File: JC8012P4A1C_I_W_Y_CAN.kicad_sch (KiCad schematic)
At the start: 16 parts, among them J1 610110249121, J2 68711414522, J3 653104131822, U1 TLE9250VSJ

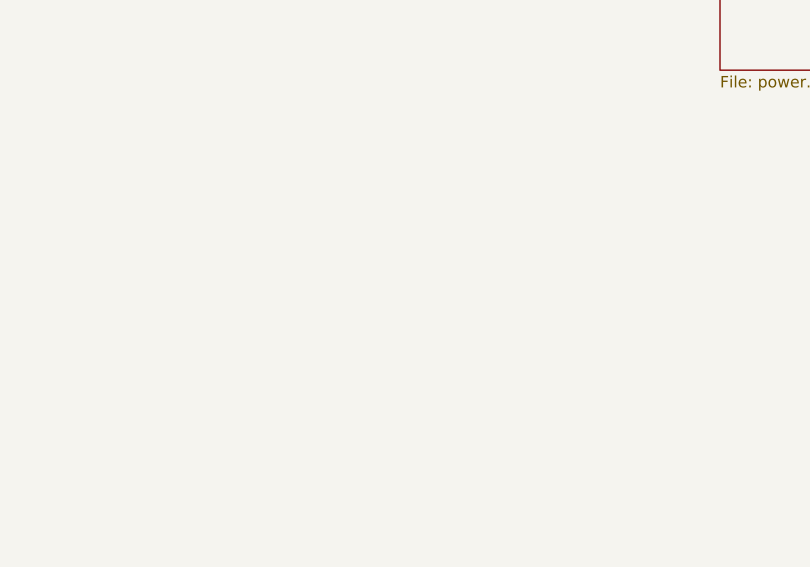
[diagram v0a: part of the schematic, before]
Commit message: Test points TP1-TP5 in the schematic
TP1 +5V, TP2 GND, TP3 CAN_H, TP4 CAN_L (main sheet), TP5 VIN_PROT
(12 V after fuse and reverse polarity protection, power sheet).
Footprint TestPoint_Pad_D1.5mm (SMD). Not yet on the PCB (F8).

Co-Authored-By: Claude Opus 5.5 <noreply@anthropic.com>
Claude-Session: https://claude.ai/code/session_014h8cGi8SRWthYdGFH1Qgzz
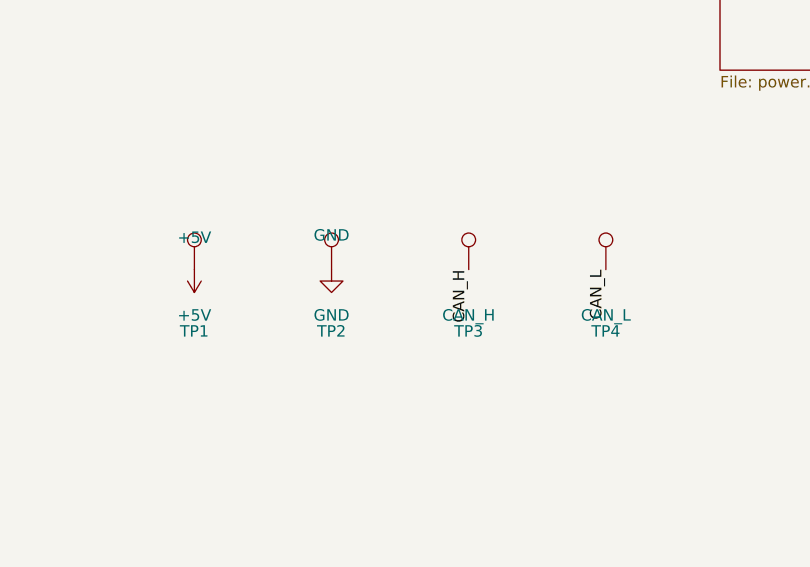
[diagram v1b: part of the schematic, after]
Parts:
- added TP1: +5V, TestPoint:TestPoint_Pad_D1.5mm, symbol Connector:TestPoint
- added TP2: GND, TestPoint:TestPoint_Pad_D1.5mm, symbol Connector:TestPoint
- added TP3: CAN_H, TestPoint:TestPoint_Pad_D1.5mm, symbol Connector:TestPoint
- added TP4: CAN_L, TestPoint:TestPoint_Pad_D1.5mm, symbol Connector:TestPoint
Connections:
- net +5V: now also TP1.1
- net CAN_H: now also TP3.1
- net CAN_L: now also TP4.1
- net GND: now also TP2.1

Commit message: Test points excluded from BOM, README: hand assembly, stencil, BOM export
Co-Authored-By: Claude Opus 5.5 <noreply@anthropic.com>
Claude-Session: https://claude.ai/code/session_014h8cGi8SRWthYdGFH1Qgzz
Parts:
- TP1, TP2, TP3, TP4: now left out of the parts list
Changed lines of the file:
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@@
 		(body_style 1)
 		(exclude_from_sim no)
-		(in_bom yes)
+		(in_bom no)
 		(on_board yes)
 		(in_pos_files yes)
@@
 		(body_style 1)
 		(exclude_from_sim no)
-		(in_bom yes)
+		(in_bom no)
 		(on_board yes)
 		(in_pos_files yes)
@@
 		(body_style 1)
 		(exclude_from_sim no)
-		(in_bom yes)
+		(in_bom no)
 		(on_board yes)
 		(in_pos_files yes)
@@
 		(body_style 1)
 		(exclude_from_sim no)
-		(in_bom yes)
-		(on_board yes)
-		(in_pos_files yes)
+		(in_bom no)
+		(on_board yes)
+		(in_pos_files yes)

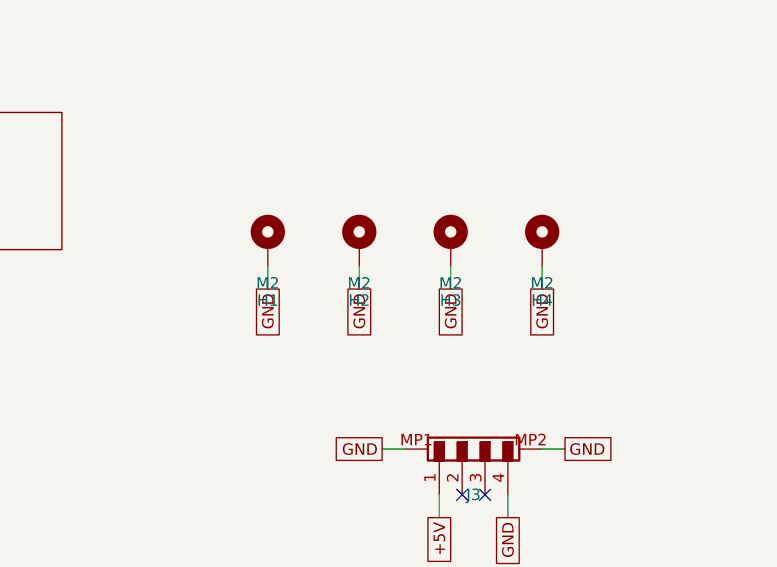
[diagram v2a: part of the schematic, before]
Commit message: Mounting holes H1-H4 replaced by SMD steel spacers Wurth 9774025943R (2.5 mm, M2x6)
Co-Authored-By: Claude Opus 5.5 <noreply@anthropic.com>
Claude-Session: https://claude.ai/code/session_014h8cGi8SRWthYdGFH1Qgzz
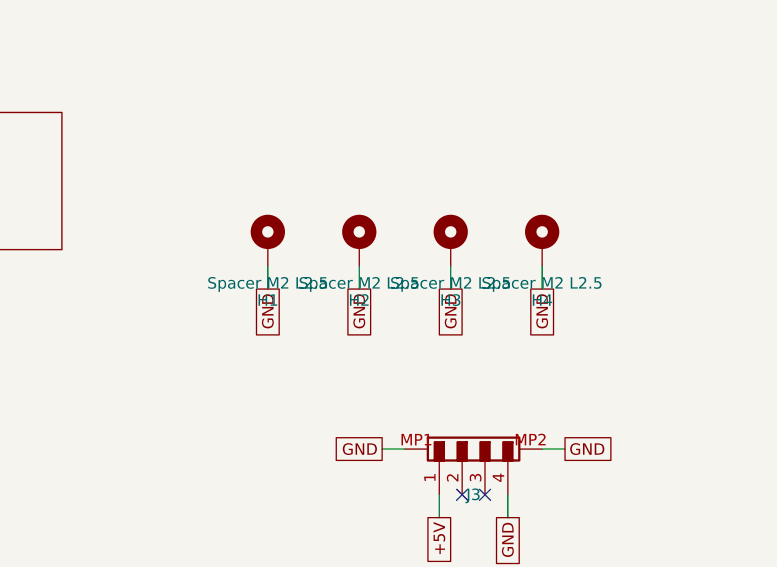
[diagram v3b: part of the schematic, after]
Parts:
- H1, H2, H3, H4: value M2 -> Spacer M2 L2.5; footprint MountingHole:MountingHole_2.2mm_M2_Pad_Via -> JC8012P4A1C_CAN:A_Wurth_WA-SMST_9774025943R; MPN (none) -> 9774025943R; Manufacturer (none) -> Wurth Elektronik; now in the parts list
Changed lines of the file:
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@@
 		(body_style 1)
 		(exclude_from_sim no)
-		(in_bom no)
+		(in_bom yes)
 		(on_board yes)
 		(in_pos_files no)
@@
 			)
 		)
-		(property "Value" "M2"
+		(property "Value" "Spacer M2 L2.5"
 			(at 213.36 133.985 0)
 			(show_name no)
@@
 			)
 		)
-		(property "Footprint" "MountingHole:MountingHole_2.2mm_M2_Pad_Via"
+		(property "Footprint" "JC8012P4A1C_CAN:A_Wurth_WA-SMST_9774025943R"
 			(at 213.36 129.54 0)
 			(hide yes)
@@
 			)
 		)
-		(property "Description" "Mounting Hole with connection"
-			(at 213.36 129.54 0)
-			(hide yes)
-			(show_name no)
-			(do_not_autoplace no)
-			(effects
-				(font
-					(size 1.27 1.27)
-				)
+		(property "Description" "SMD steel spacer, through hole 2.25 mm, L 2.5 mm, for M2x6 screw"
+			(at 213.36 129.54 0)
+			(hide yes)
+			(show_name no)
+			(do_not_autoplace no)
+			(effects
+				(font
+					(size 1.27 1.27)
+				)
+			)
+		)
+		(property "MPN" "9774025943R"
+			(at 213.36 129.54 0)
+			(effects
+				(font
+					(size 1.27 1.27)
+				)
+				(hide yes)
+			)
+		)
+		(property "Manufacturer" "Wurth Elektronik"
+			(at 213.36 129.54 0)
+			(effects
+				(font
+					(size 1.27 1.27)
+				)
+				(hide yes)
 			)
 		)
@@
 		(body_style 1)
 		(exclude_from_sim no)
-		(in_bom no)
+		(in_bom yes)
 		(on_board yes)
 		(in_pos_files no)
@@
 			)
 		)
-		(property "Value" "M2"
+		(property "Value" "Spacer M2 L2.5"
 			(at 223.52 133.985 0)
 			(show_name no)
@@
 			)
 		)
-		(property "Footprint" "MountingHole:MountingHole_2.2mm_M2_Pad_Via"
+		(property "Footprint" "JC8012P4A1C_CAN:A_Wurth_WA-SMST_9774025943R"
 			(at 223.52 129.54 0)
 			(hide yes)
@@
 			)
 		)
-		(property "Description" "Mounting Hole with connection"
-			(at 223.52 129.54 0)
-			(hide yes)
-			(show_name no)
-			(do_not_autoplace no)
-			(effects
-				(font
-					(size 1.27 1.27)
-				)
+		(property "Description" "SMD steel spacer, through hole 2.25 mm, L 2.5 mm, for M2x6 screw"
+			(at 223.52 129.54 0)
+			(hide yes)
+			(show_name no)
+			(do_not_autoplace no)
+			(effects
+				(font
+					(size 1.27 1.27)
+				)
+			)
+		)
+		(property "MPN" "9774025943R"
+			(at 223.52 129.54 0)
+			(effects
+				(font
+					(size 1.27 1.27)
+				)
+				(hide yes)
+			)
+		)
+		(property "Manufacturer" "Wurth Elektronik"
+			(at 223.52 129.54 0)
+			(effects
+				(font
+					(size 1.27 1.27)
+				)
+				(hide yes)
 			)
 		)
@@
 		(body_style 1)
 		(exclude_from_sim no)
-		(in_bom no)
+		(in_bom yes)
 		(on_board yes)
 		(in_pos_files no)
@@
 			)
 		)
-		(property "Value" "M2"
+		(property "Value" "Spacer M2 L2.5"
 			(at 233.68 133.985 0)
 			(show_name no)
@@
 			)
 		)
-		(property "Footprint" "MountingHole:MountingHole_2.2mm_M2_Pad_Via"
+		(property "Footprint" "JC8012P4A1C_CAN:A_Wurth_WA-SMST_9774025943R"
 			(at 233.68 129.54 0)
 			(hide yes)
@@
 			)
 		)
-		(property "Description" "Mounting Hole with connection"
-			(at 233.68 129.54 0)
-			(hide yes)
-			(show_name no)
-			(do_not_autoplace no)
-			(effects
-				(font
-					(size 1.27 1.27)
-				)
+		(property "Description" "SMD steel spacer, through hole 2.25 mm, L 2.5 mm, for M2x6 screw"
+			(at 233.68 129.54 0)
+			(hide yes)
+			(show_name no)
+			(do_not_autoplace no)
+			(effects
+				(font
+					(size 1.27 1.27)
+				)
+			)
+		)
+		(property "MPN" "9774025943R"
+			(at 233.68 129.54 0)
+			(effects
+				(font
+					(size 1.27 1.27)
+				)
+				(hide yes)
+			)
+		)
+		(property "Manufacturer" "Wurth Elektronik"
+			(at 233.68 129.54 0)
+			(effects
+				(font
+					(size 1.27 1.27)
+				)
+				(hide yes)
 			)
 		)
@@
 		(body_style 1)
 		(exclude_from_sim no)
-		(in_bom no)
+		(in_bom yes)
 		(on_board yes)
 		(in_pos_files no)
@@
 			)
 		)
-		(property "Value" "M2"
+		(property "Value" "Spacer M2 L2.5"
 			(at 243.84 133.985 0)
 			(show_name no)
@@
 			)
 		)
-		(property "Footprint" "MountingHole:MountingHole_2.2mm_M2_Pad_Via"
+		(property "Footprint" "JC8012P4A1C_CAN:A_Wurth_WA-SMST_9774025943R"
 			(at 243.84 129.54 0)
 			(hide yes)
@@
 			)
 		)
-		(property "Description" "Mounting Hole with connection"
-			(at 243.84 129.54 0)
-			(hide yes)
-			(show_name no)
-			(do_not_autoplace no)
-			(effects
-				(font
-					(size 1.27 1.27)
-				)
-			)
-		)
+		(property "Description" "SMD steel spacer, through hole 2.25 mm, L 2.5 mm, for M2x6 screw"
+			(at 243.84 129.54 0)
+			(hide yes)
+			(show_name no)
+			(do_not_autoplace no)
+			(effects
+				(font
+					(size 1.27 1.27)
+				)
+			)
+		)
+		(property "MPN" "9774025943R"
+			(at 243.84 129.54 0)
+			(effects
+				(font
+					(size 1.27 1.27)
+				)
+				(hide yes)
+			)
+		)
+		(property "Manufacturer" "Wurth Elektronik"
+			(at 243.84 129.54 0)
+			(effects
+				(font
+					(size 1.27 1.27)
+				)
+				(hide yes)
+			)
+		)
